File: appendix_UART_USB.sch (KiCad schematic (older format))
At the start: 28 parts, among them J504 USB_C_Receptacle, U1 USBLC6-2SC6, U502 FT2232D, X501 SG5032CCN-6.000000M-HJGA3

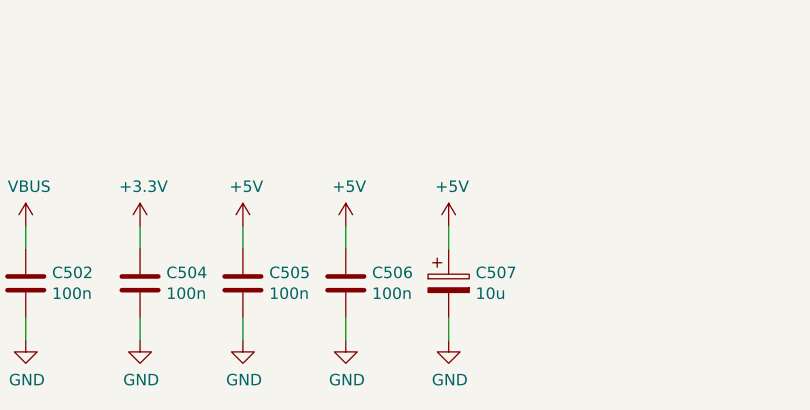
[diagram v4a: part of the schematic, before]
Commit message: TVS protection, BOOT1 pin, user BTN
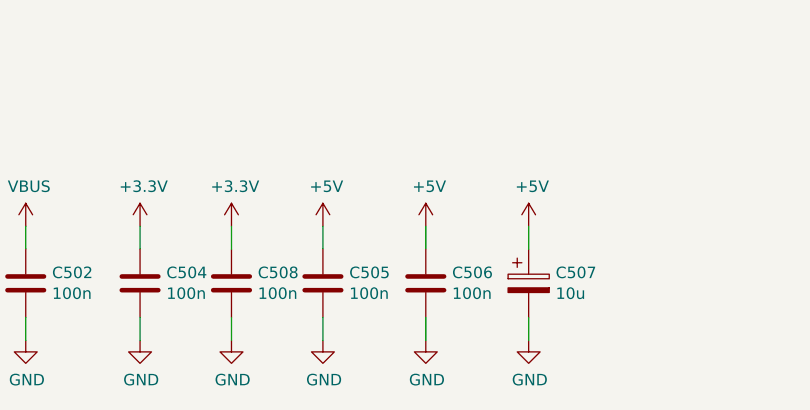
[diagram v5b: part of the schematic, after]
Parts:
- added C508: 100n, Capacitors_SMD:C_0603, symbol Device:C
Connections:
- net +3V3: now also C508.1
- net GND: now also C508.2
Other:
- moved on the sheet: C505, C506, C507
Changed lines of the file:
@@
 L Device:C C505
 U 1 1 5CD79248
-P 2400 6950
-F 0 "C505" H 2515 6996 50  0000 L CNN
-F 1 "100n" H 2515 6905 50  0000 L CNN
-F 2 "Capacitors_SMD:C_0603" H 2438 6800 50  0001 C CNN
-F 3 "~" H 2400 6950 50  0001 C CNN
-	1    2400 6950
+P 2750 6950
+F 0 "C505" H 2865 6996 50  0000 L CNN
+F 1 "100n" H 2865 6905 50  0000 L CNN
+F 2 "Capacitors_SMD:C_0603" H 2788 6800 50  0001 C CNN
+F 3 "~" H 2750 6950 50  0001 C CNN
+	1    2750 6950
 	1    0    0    -1
 $EndComp
@@
 L power:GND #PWR0513
 U 1 1 5CD79252
-P 2400 7200
-F 0 "#PWR0513" H 2400 6950 50  0001 C CNN
-F 1 "GND" H 2405 7027 50  0000 C CNN
-F 2 "" H 2400 7200 50  0001 C CNN
-F 3 "" H 2400 7200 50  0001 C CNN
-	1    2400 7200
-	1    0    0    -1
-$EndComp
-Wire Wire Line
-	2400 6800 2400 6700
-Wire Wire Line
-	2400 7200 2400 7100
+P 2750 7200
+F 0 "#PWR0513" H 2750 6950 50  0001 C CNN
+F 1 "GND" H 2755 7027 50  0000 C CNN
+F 2 "" H 2750 7200 50  0001 C CNN
+F 3 "" H 2750 7200 50  0001 C CNN
+	1    2750 7200
+	1    0    0    -1
+$EndComp
+Wire Wire Line
+	2750 6800 2750 6700
+Wire Wire Line
+	2750 7200 2750 7100
 $Comp
 L Device:C C506
 U 1 1 5CD7CE0B
-P 2850 6950
-F 0 "C506" H 2965 6996 50  0000 L CNN
-F 1 "100n" H 2965 6905 50  0000 L CNN
-F 2 "Capacitors_SMD:C_0603" H 2888 6800 50  0001 C CNN
-F 3 "~" H 2850 6950 50  0001 C CNN
-	1    2850 6950
+P 3200 6950
+F 0 "C506" H 3315 6996 50  0000 L CNN
+F 1 "100n" H 3315 6905 50  0000 L CNN
+F 2 "Capacitors_SMD:C_0603" H 3238 6800 50  0001 C CNN
+F 3 "~" H 3200 6950 50  0001 C CNN
+	1    3200 6950
 	1    0    0    -1
 $EndComp
@@
 L power:GND #PWR0514
 U 1 1 5CD7CE15
-P 2850 7200
-F 0 "#PWR0514" H 2850 6950 50  0001 C CNN
-F 1 "GND" H 2855 7027 50  0000 C CNN
-F 2 "" H 2850 7200 50  0001 C CNN
-F 3 "" H 2850 7200 50  0001 C CNN
-	1    2850 7200
-	1    0    0    -1
-$EndComp
-Wire Wire Line
-	2850 6800 2850 6700
-Wire Wire Line
-	2850 7200 2850 7100
+P 3200 7200
+F 0 "#PWR0514" H 3200 6950 50  0001 C CNN
+F 1 "GND" H 3205 7027 50  0000 C CNN
+F 2 "" H 3200 7200 50  0001 C CNN
+F 3 "" H 3200 7200 50  0001 C CNN
+	1    3200 7200
+	1    0    0    -1
+$EndComp
+Wire Wire Line
+	3200 6800 3200 6700
+Wire Wire Line
+	3200 7200 3200 7100
 $Comp
 L power:GND #PWR0515
 U 1 1 5CD80C48
-P 3300 7200
-F 0 "#PWR0515" H 3300 6950 50  0001 C CNN
-F 1 "GND" H 3305 7027 50  0000 C CNN
-F 2 "" H 3300 7200 50  0001 C CNN
-F 3 "" H 3300 7200 50  0001 C CNN
-	1    3300 7200
-	1    0    0    -1
-$EndComp
-Wire Wire Line
-	3300 6800 3300 6700
-Wire Wire Line
-	3300 7200 3300 7100
+P 3650 7200
+F 0 "#PWR0515" H 3650 6950 50  0001 C CNN
+F 1 "GND" H 3655 7027 50  0000 C CNN
+F 2 "" H 3650 7200 50  0001 C CNN
+F 3 "" H 3650 7200 50  0001 C CNN
+	1    3650 7200
+	1    0    0    -1
+$EndComp
+Wire Wire Line
+	3650 6800 3650 6700
+Wire Wire Line
+	3650 7200 3650 7100
 $Comp
 L Device:CP C507
 U 1 1 5CD84D48
-P 3300 6950
-F 0 "C507" H 3418 6996 50  0000 L CNN
-F 1 "10u" H 3418 6905 50  0000 L CNN
-F 2 "Capacitors_SMD:C_1210" H 3338 6800 50  0001 C CNN
-F 3 "~" H 3300 6950 50  0001 C CNN
-	1    3300 6950
+P 3650 6950
+F 0 "C507" H 3768 6996 50  0000 L CNN
+F 1 "10u" H 3768 6905 50  0000 L CNN
+F 2 "Capacitors_SMD:C_1210" H 3688 6800 50  0001 C CNN
+F 3 "~" H 3650 6950 50  0001 C CNN
+	1    3650 6950
 	1    0    0    -1
 $EndComp
@@
 L power:+5V #PWR06
 U 1 1 5CBC8577
-P 2400 6700
-F 0 "#PWR06" H 2400 6550 50  0001 C CNN
-F 1 "+5V" H 2415 6873 50  0000 C CNN
-F 2 "" H 2400 6700 50  0001 C CNN
-F 3 "" H 2400 6700 50  0001 C CNN
-	1    2400 6700
+P 2750 6700
+F 0 "#PWR06" H 2750 6550 50  0001 C CNN
+F 1 "+5V" H 2765 6873 50  0000 C CNN
+F 2 "" H 2750 6700 50  0001 C CNN
+F 3 "" H 2750 6700 50  0001 C CNN
+	1    2750 6700
 	1    0    0    -1
 $EndComp
@@
 L power:+5V #PWR07
 U 1 1 5CBC9FB7
-P 2850 6700
-F 0 "#PWR07" H 2850 6550 50  0001 C CNN
-F 1 "+5V" H 2865 6873 50  0000 C CNN
-F 2 "" H 2850 6700 50  0001 C CNN
-F 3 "" H 2850 6700 50  0001 C CNN
-	1    2850 6700
+P 3200 6700
+F 0 "#PWR07" H 3200 6550 50  0001 C CNN
+F 1 "+5V" H 3215 6873 50  0000 C CNN
+F 2 "" H 3200 6700 50  0001 C CNN
+F 3 "" H 3200 6700 50  0001 C CNN
+	1    3200 6700
 	1    0    0    -1
 $EndComp
@@
 L power:+5V #PWR08
 U 1 1 5CBCA403
-P 3300 6700
-F 0 "#PWR08" H 3300 6550 50  0001 C CNN
-F 1 "+5V" H 3315 6873 50  0000 C CNN
-F 2 "" H 3300 6700 50  0001 C CNN
-F 3 "" H 3300 6700 50  0001 C CNN
-	1    3300 6700
+P 3650 6700
+F 0 "#PWR08" H 3650 6550 50  0001 C CNN
+F 1 "+5V" H 3665 6873 50  0000 C CNN
+F 2 "" H 3650 6700 50  0001 C CNN
+F 3 "" H 3650 6700 50  0001 C CNN
+	1    3650 6700
 	1    0    0    -1
 $EndComp
@@
 Text HLabel 8200 1650 2    50   Input ~ 0
 FT_TX_A
+$Comp
+L Device:C C508
+U 1 1 5D7F38AC
+P 2350 6950
+F 0 "C508" H 2465 6996 50  0000 L CNN
+F 1 "100n" H 2465 6905 50  0000 L CNN
+F 2 "Capacitors_SMD:C_0603" H 2388 6800 50  0001 C CNN
+F 3 "~" H 2350 6950 50  0001 C CNN
+	1    2350 6950
+	1    0    0    -1
+$EndComp
+$Comp
+L power:GND #PWR0517
+U 1 1 5D7F38B6
+P 2350 7200
+F 0 "#PWR0517" H 2350 6950 50  0001 C CNN
+F 1 "GND" H 2355 7027 50  0000 C CNN
+F 2 "" H 2350 7200 50  0001 C CNN
+F 3 "" H 2350 7200 50  0001 C CNN
+	1    2350 7200
+	1    0    0    -1
+$EndComp
+Wire Wire Line
+	2350 6800 2350 6700
+Wire Wire Line
+	2350 7200 2350 7100
+$Comp
+L power:+3.3V #PWR0516
+U 1 1 5D7F38C2
+P 2350 6700
+F 0 "#PWR0516" H 2350 6550 50  0001 C CNN
+F 1 "+3.3V" H 2365 6873 50  0000 C CNN
+F 2 "" H 2350 6700 50  0001 C CNN
+F 3 "" H 2350 6700 50  0001 C CNN
+	1    2350 6700
+	1    0    0    -1
+$EndComp
 $EndSCHEMATC

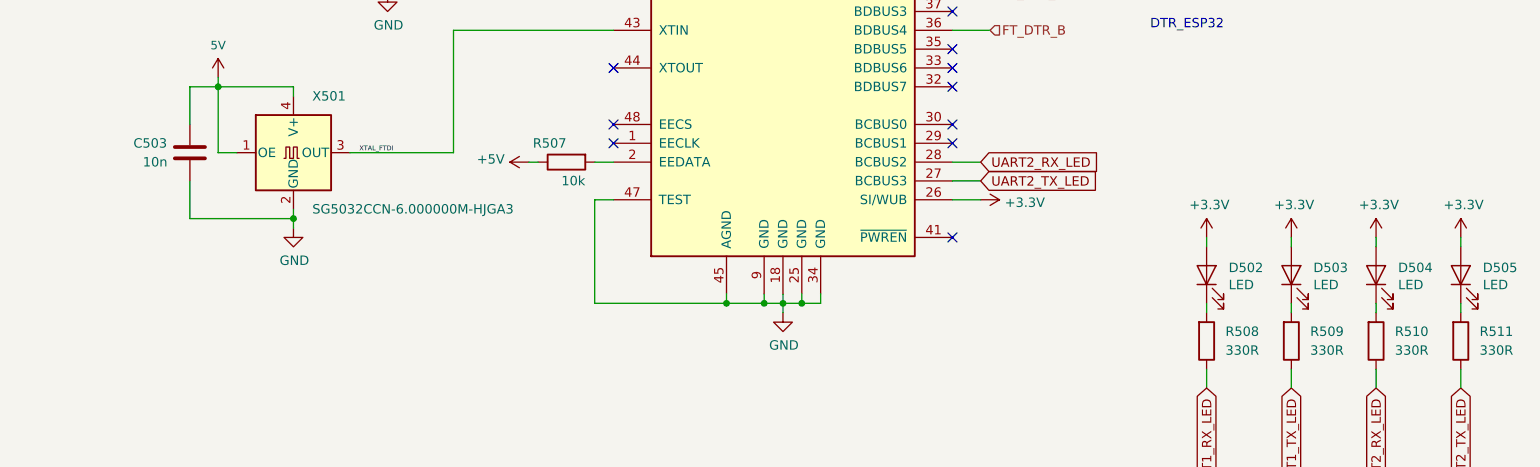
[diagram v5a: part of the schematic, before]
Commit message: added comments from comments branch corrected silk Servo2 added title to schematic pages
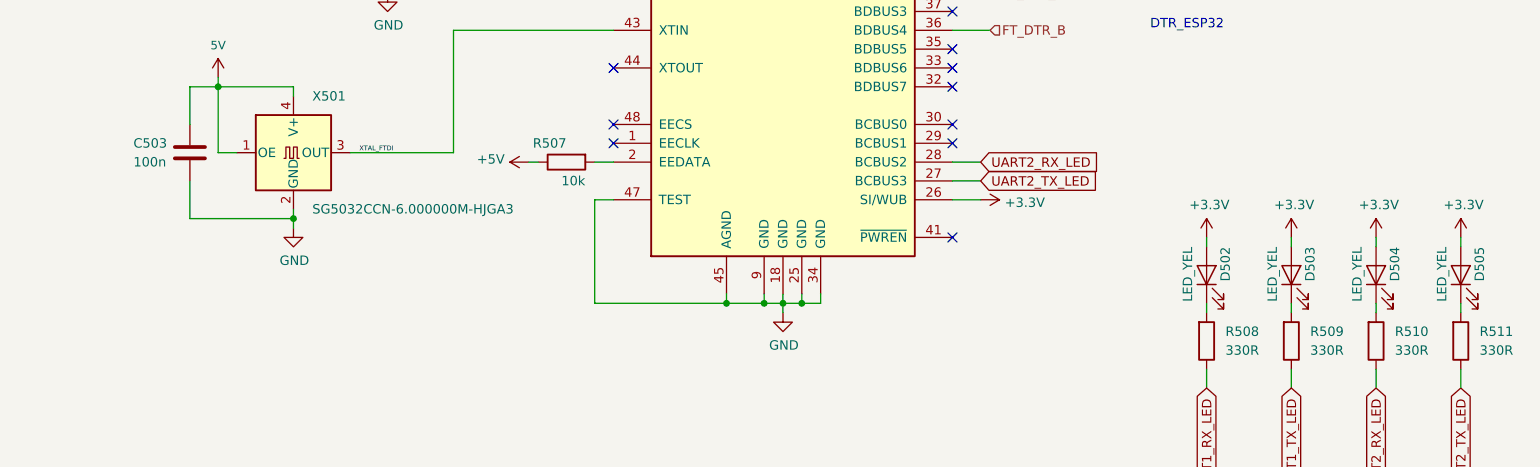
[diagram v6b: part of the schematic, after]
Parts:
- C503: value 10n -> 100n
- D502, D503, D504, D505: value LED -> LED_YEL
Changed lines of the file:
@@
 Sheet 5 6
 Title "USB to UART Interface"
-Date ""
-Rev "1"
-Comp ""
+Date "2019-05-10"
+Rev "1.1"
+Comp "FHNW University of Applied Sciences"
 Comment1 "EIT Pro4 FS19 Team 8"
 Comment2 ""
@@
 AR Path="/5CC68B5F" Ref="D?"  Part="1"
 AR Path="/5CA3CC17/5CC68B5F" Ref="D502"  Part="1"
-F 0 "D502" V 9389 4733 50  0000 R CNN
-F 1 "LED" V 9298 4733 50  0000 R CNN
+F 0 "D502" H 9500 4750 50  0000 R CNN
+F 1 "LED_YEL" H 9500 4950 50  0000 R CNN
 F 2 "LED_SMD:LED_0805_2012Metric" H 9350 4850 50  0001 C CNN
 F 3 "~" H 9350 4850 50  0001 C CNN
@@
 AR Path="/5CC8BE19" Ref="D?"  Part="1"
 AR Path="/5CA3CC17/5CC8BE19" Ref="D503"  Part="1"
-F 0 "D503" V 9839 4733 50  0000 R CNN
-F 1 "LED" V 9748 4733 50  0000 R CNN
+F 0 "D503" H 9950 4750 50  0000 R CNN
+F 1 "LED_YEL" H 9950 4950 50  0000 R CNN
 F 2 "LED_SMD:LED_0805_2012Metric" H 9800 4850 50  0001 C CNN
 F 3 "~" H 9800 4850 50  0001 C CNN
@@
 AR Path="/5CC90F6E" Ref="D?"  Part="1"
 AR Path="/5CA3CC17/5CC90F6E" Ref="D504"  Part="1"
-F 0 "D504" V 10289 4733 50  0000 R CNN
-F 1 "LED" V 10198 4733 50  0000 R CNN
+F 0 "D504" H 10400 4750 50  0000 R CNN
+F 1 "LED_YEL" H 10400 4950 50  0000 R CNN
 F 2 "LED_SMD:LED_0805_2012Metric" H 10250 4850 50  0001 C CNN
 F 3 "~" H 10250 4850 50  0001 C CNN
@@
 AR Path="/5CC90F8F" Ref="D?"  Part="1"
 AR Path="/5CA3CC17/5CC90F8F" Ref="D505"  Part="1"
-F 0 "D505" V 10739 4733 50  0000 R CNN
-F 1 "LED" V 10648 4733 50  0000 R CNN
+F 0 "D505" H 10850 4750 50  0000 R CNN
+F 1 "LED_YEL" H 10850 4950 50  0000 R CNN
 F 2 "LED_SMD:LED_0805_2012Metric" H 10700 4850 50  0001 C CNN
 F 3 "~" H 10700 4850 50  0001 C CNN
@@
 P 3950 4200
 F 0 "C503" H 3650 4250 50  0000 L CNN
-F 1 "10n" H 3700 4150 50  0000 L CNN
+F 1 "100n" H 3650 4150 50  0000 L CNN
 F 2 "Capacitors_SMD:C_0603" H 3988 4050 50  0001 C CNN
 F 3 "~" H 3950 4200 50  0001 C CNN
